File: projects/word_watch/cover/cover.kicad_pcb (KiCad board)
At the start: 2 copper layers, 36 x 36 mm, 0 parts

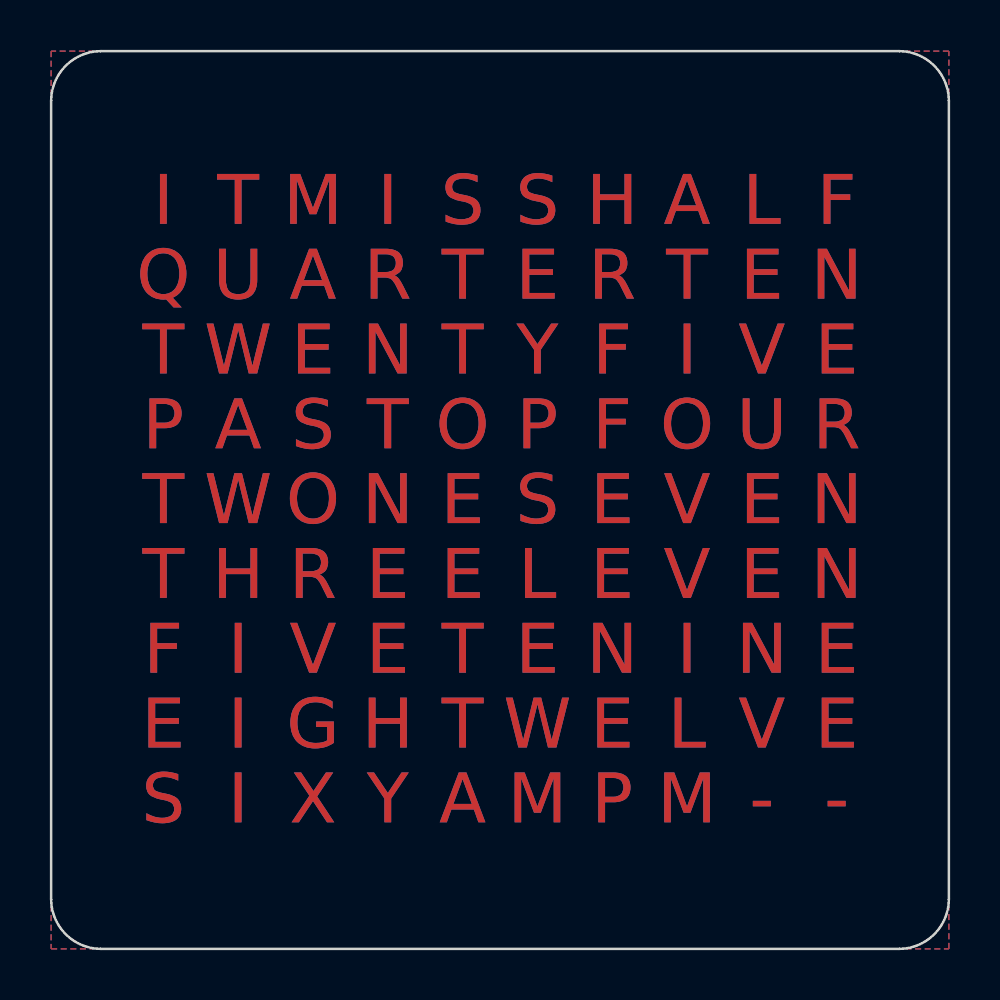
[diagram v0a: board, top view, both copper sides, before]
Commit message: update word_watch cover
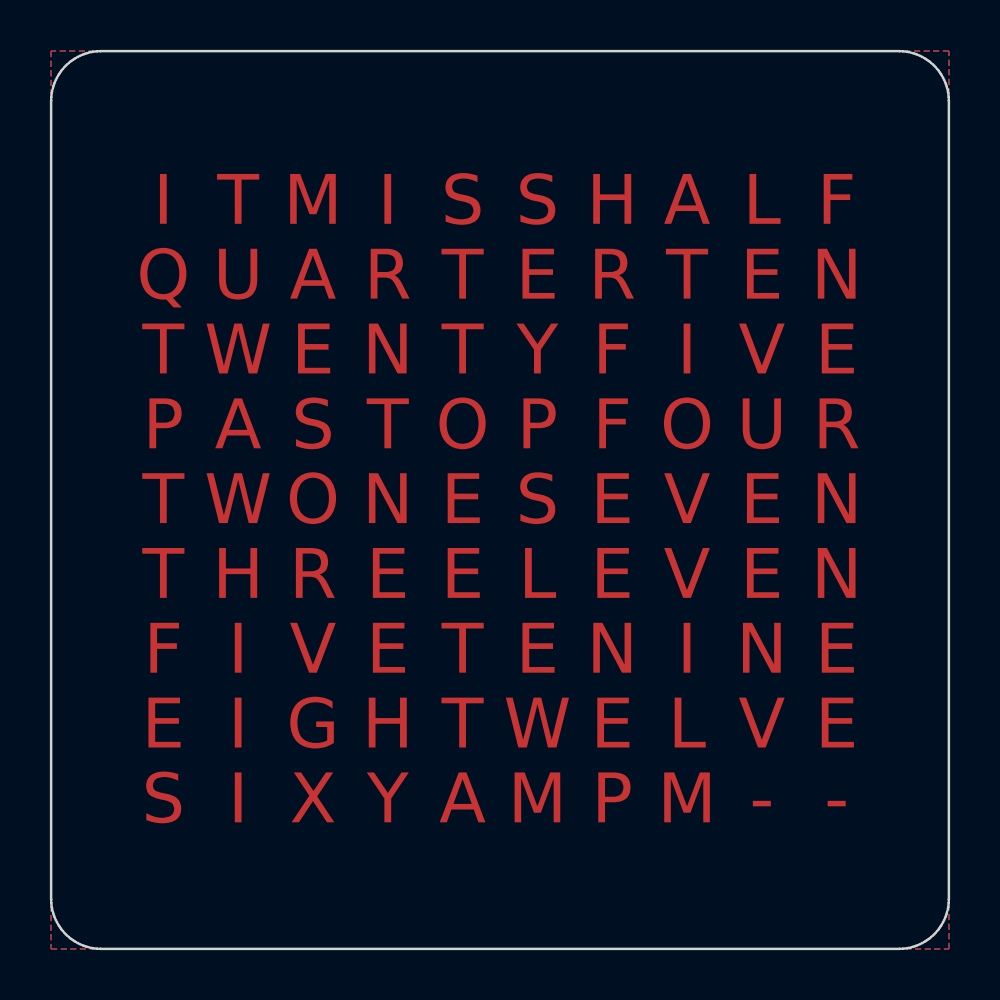
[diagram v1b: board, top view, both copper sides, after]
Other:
- board text added: "no amount of money ever bought a second of time."
- board text added: "word watch"
